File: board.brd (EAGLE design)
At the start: 52 x 53 mm, 14 parts, among them J1 5.5x2.1mm Barrel, T1 TIP122

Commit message: Updated with Gerber files
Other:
- board size 52 x 53 mm -> 52 x 51.7 mm
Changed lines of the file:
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@@
 <plain>
 <wire x1="0" y1="-12.7" x2="52.05" y2="-12.7" width="0" layer="20"/>
-<wire x1="52.05" y1="-12.7" x2="52.05" y2="40.31" width="0" layer="20"/>
-<wire x1="52.05" y1="40.31" x2="0" y2="40.31" width="0" layer="20"/>
-<wire x1="0" y1="40.31" x2="0" y2="-12.7" width="0" layer="20"/>
+<wire x1="52.05" y1="-12.7" x2="52.05" y2="39.04" width="0" layer="20"/>
+<wire x1="52.05" y1="39.04" x2="0" y2="39.04" width="0" layer="20"/>
+<wire x1="0" y1="39.04" x2="0" y2="-12.7" width="0" layer="20"/>
 </plain>
 <attributes>

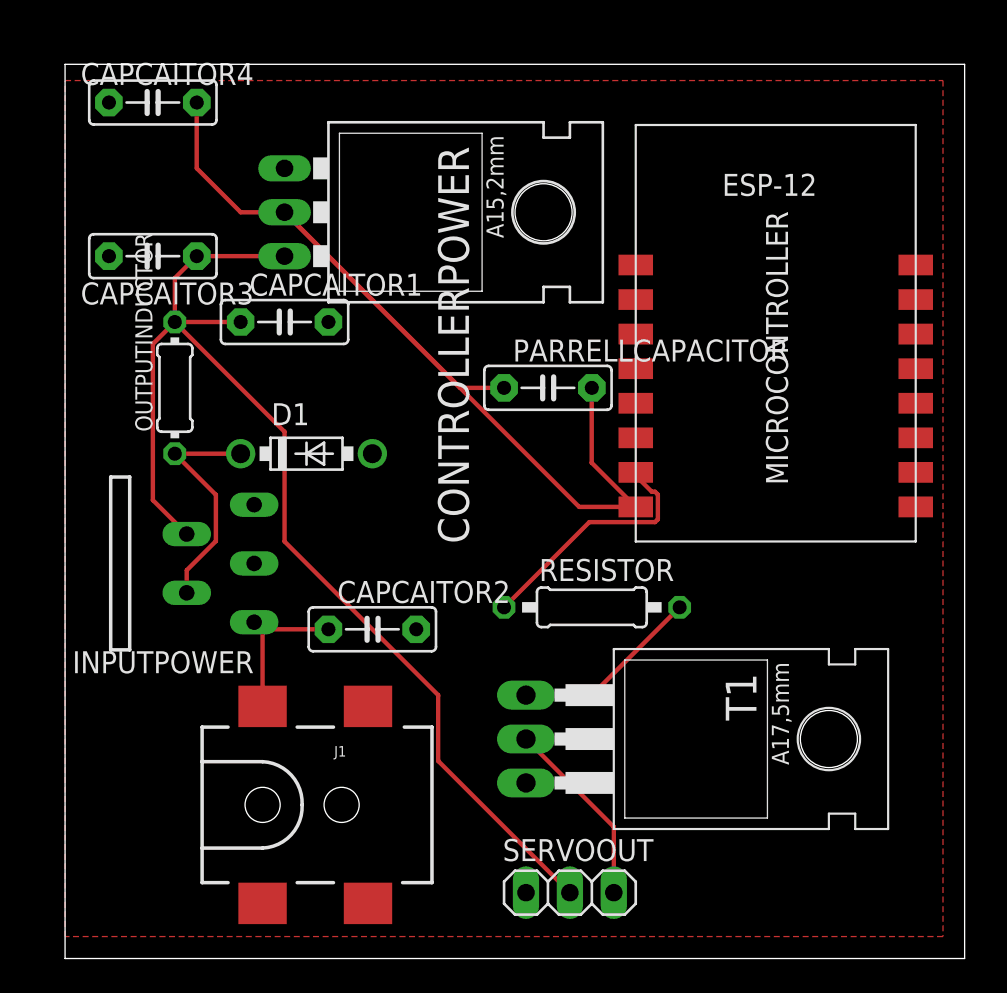
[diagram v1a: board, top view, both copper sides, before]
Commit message: Change base board to esp 01
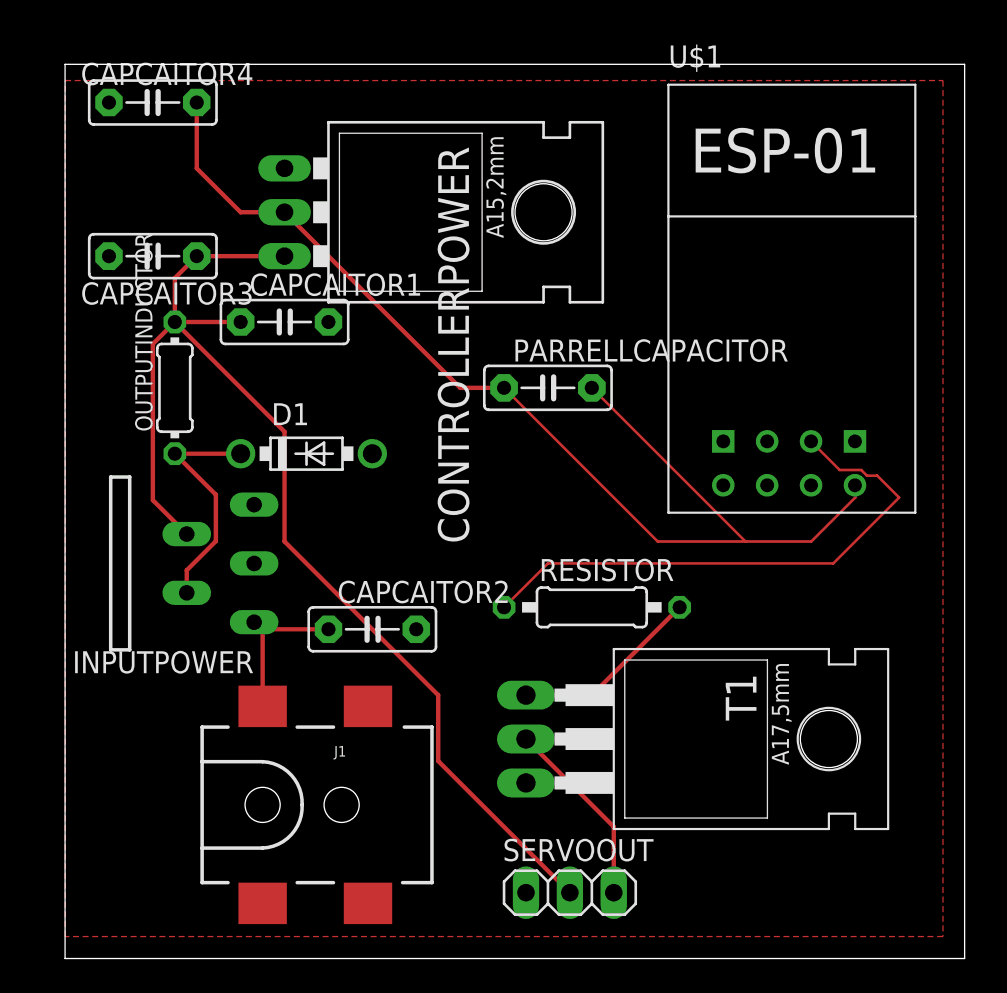
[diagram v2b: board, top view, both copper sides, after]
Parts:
- removed MICROCONTROLLER: ESP8266_ESP-12, ESP8266-ESP12:ESP8266-ESP12
- added U$1: ESP01, esp8266modules:ESP01
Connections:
- net GND: now also U$1.GND; no longer MICROCONTROLLER.1
- net N$7: now also U$1.VCC; no longer MICROCONTROLLER.16
- net N$9: now also U$1.GPIO0; no longer MICROCONTROLLER.15
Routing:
- net N$9: track 14.7 -> 31.9 mm
- net N$7: track 62.2 -> 65.2 mm
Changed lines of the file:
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@@
 <attribute name="VALUE" x="10.668" y="21.336" size="1.27" layer="27" ratio="10"/>
-</element>
-<element name="MICROCONTROLLER" library="ESP8266-ESP12" package="ESP8266-ESP12" value="ESP8266_ESP-12" x="33.02" y="11.43" smashed="yes">
-<attribute name="NAME" x="41.83" y="14.7" size="1.27" layer="21" rot="R90"/>
 </element>
 <element name="CONTROLLERPOWER" library="LD1117V33" package="LD1117V33" value="LD1117V33" x="21.59" y="30.48" smashed="yes" rot="R270">
@@
 <attribute name="VALUE" x="25.908" y="17.526" size="1.27" layer="27" ratio="10"/>
 </element>
+<element name="U$1" library="esp8266modules" package="ESP01" value="ESP01" x="41.91" y="22.86" smashed="yes">
+<attribute name="NAME" x="34.91" y="38.86" size="1.27" layer="25"/>
+<attribute name="VALUE" x="34.91" y="11.86" size="1.27" layer="27"/>
+</element>
 </elements>
 <signals>
@@
 <contactref element="CAPCAITOR3" pad="2"/>
 <contactref element="CAPCAITOR4" pad="2"/>
-<contactref element="MICROCONTROLLER" pad="1"/>
 <contactref element="SERVOOUT" pad="1"/>
 <contactref element="J1" pad="GND"/>
-<contactref element="T1" pad="3"/>
 <polygon width="0.254" layer="1">
 <vertex x="0" y="38.1"/>
@@
 </polygon>
 <contactref element="D1" pad="A"/>
+<contactref element="T1" pad="3"/>
+<contactref element="U$1" pad="GND"/>
 </signal>
 <signal name="N$3">
@@
 <contactref element="CONTROLLERPOWER" pad="OUT"/>
 <contactref element="CAPCAITOR4" pad="1"/>
-<contactref element="MICROCONTROLLER" pad="16"/>
 <wire x1="12.7" y1="30.48" x2="10.16" y2="30.48" width="0.254" layer="1"/>
 <wire x1="10.16" y1="30.48" x2="7.62" y2="33.02" width="0.254" layer="1"/>
 <wire x1="7.62" y1="33.02" x2="7.62" y2="36.83" width="0.254" layer="1"/>
 <contactref element="PARRELLCAPACITOR" pad="1"/>
-<contactref element="PARRELLCAPACITOR" pad="2"/>
-<wire x1="12.7" y1="30.48" x2="29.75" y2="13.43" width="0.254" layer="1"/>
-<wire x1="29.75" y1="13.43" x2="33.02" y2="13.43" width="0.254" layer="1"/>
 <wire x1="12.7" y1="30.48" x2="22.86" y2="20.32" width="0.254" layer="1"/>
 <wire x1="22.86" y1="20.32" x2="25.4" y2="20.32" width="0.254" layer="1"/>
-<wire x1="33.02" y1="13.43486875" x2="33.02" y2="13.43" width="0.254" layer="1"/>
-<wire x1="30.4706" y1="15.98426875" x2="33.02" y2="13.43486875" width="0.254" layer="1"/>
-<wire x1="30.48" y1="20.32" x2="30.4706" y2="20.3106" width="0.254" layer="1"/>
-<wire x1="30.4706" y1="20.3106" x2="30.4706" y2="15.98426875" width="0.254" layer="1"/>
+<contactref element="U$1" pad="VCC"/>
+<contactref element="PARRELLCAPACITOR" pad="2"/>
+<wire x1="30.48" y1="20.32" x2="39.37" y2="11.43" width="0.1524" layer="1"/>
+<wire x1="39.37" y1="11.43" x2="43.18" y2="11.43" width="0.1524" layer="1"/>
+<wire x1="43.18" y1="11.43" x2="45.72" y2="13.97" width="0.1524" layer="1"/>
+<wire x1="45.72" y1="13.97" x2="45.72" y2="14.6675" width="0.1524" layer="1"/>
+<wire x1="45.72" y1="14.6675" x2="45.705" y2="14.6825" width="0.1524" layer="1"/>
+<wire x1="25.4" y1="20.32" x2="34.29" y2="11.43" width="0.1524" layer="1"/>
+<wire x1="34.29" y1="11.43" x2="39.37" y2="11.43" width="0.1524" layer="1"/>
 </signal>
 <signal name="N$8">
@@
 <wire x1="26.67" y1="2.54" x2="30.48" y2="2.54" width="0.254" layer="1"/>
 </signal>
-<signal name="N$9">
-<contactref element="RESISTOR" pad="1"/>
-<contactref element="MICROCONTROLLER" pad="15"/>
-<wire x1="33.02" y1="15.43" x2="33.21" y2="15.43" width="0.254" layer="1"/>
-<wire x1="25.4" y1="7.81" x2="25.4" y2="7.62" width="0.254" layer="1"/>
-<wire x1="33.02" y1="15.43" x2="33.02" y2="15.24" width="0.254" layer="1"/>
-<wire x1="34.13573125" y1="14.3094" x2="34.2994" y2="14.14573125" width="0.254" layer="1"/>
-<wire x1="34.2994" y1="14.14573125" x2="34.2994" y2="12.71426875" width="0.254" layer="1"/>
-<wire x1="34.2994" y1="12.71426875" x2="34.13573125" y2="12.5506" width="0.254" layer="1"/>
-<wire x1="33.02" y1="15.24" x2="33.9506" y2="14.3094" width="0.254" layer="1"/>
-<wire x1="33.9506" y1="14.3094" x2="34.13573125" y2="14.3094" width="0.254" layer="1"/>
-<wire x1="30.3306" y1="12.5506" x2="25.4" y2="7.62" width="0.254" layer="1"/>
-<wire x1="34.13573125" y1="12.5506" x2="30.3306" y2="12.5506" width="0.254" layer="1"/>
-</signal>
 <signal name="N$10">
 <contactref element="T1" pad="2"/>
@@
 <wire x1="31.75" y1="-5.08" x2="31.75" y2="-8.89" width="0.254" layer="1"/>
 </signal>
+<signal name="N$9">
+<contactref element="RESISTOR" pad="1"/>
+<contactref element="U$1" pad="GPIO0"/>
+<wire x1="46.0705875" y1="15.5651" x2="46.3956875" y2="15.24" width="0.1524" layer="1"/>
+<wire x1="46.3956875" y1="15.24" x2="46.99" y2="15.24" width="0.1524" layer="1"/>
+<wire x1="43.165" y1="17.2225" x2="44.8224" y2="15.5651" width="0.1524" layer="1"/>
+<wire x1="44.8224" y1="15.5651" x2="46.0705875" y2="15.5651" width="0.1524" layer="1"/>
+<wire x1="46.99" y1="15.24" x2="48.26" y2="13.97" width="0.1524" layer="1"/>
+<wire x1="48.26" y1="13.97" x2="44.45" y2="10.16" width="0.1524" layer="1"/>
+<wire x1="44.45" y1="10.16" x2="27.94" y2="10.16" width="0.1524" layer="1"/>
+<wire x1="27.94" y1="10.16" x2="25.4" y2="7.62" width="0.1524" layer="1"/>
+</signal>
 </signals>

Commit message: Board update and autocad update to add nx files
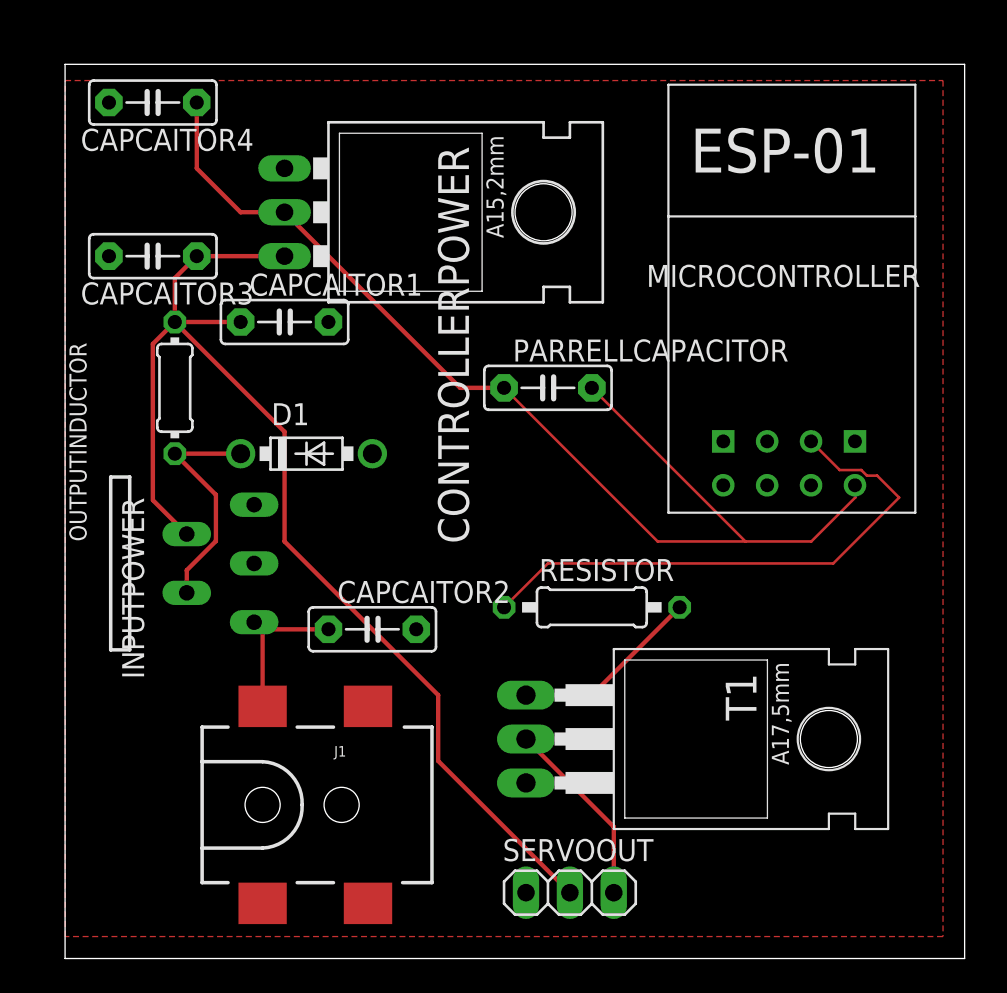
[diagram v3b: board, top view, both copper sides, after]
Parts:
- renumbered U$1 to MICROCONTROLLER
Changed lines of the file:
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@@
 <?xml version="1.0" encoding="utf-8"?>
 <!DOCTYPE eagle SYSTEM "eagle.dtd">
-<eagle version="9.2.2">
+<eagle version="9.2.0">
 <drawing>
 <settings>
@@
 </autorouter>
 <elements>
-<element name="INPUTPOWER" library="lm2575" package="TO220-5" value="LM2575-5.0T" x="2.54" y="10.16" smashed="yes" rot="R90">
-<attribute name="NAME" x="10.922" y="5.08" size="1.27" layer="25" rot="R180"/>
+<element name="INPUTPOWER" library="lm2575" package="TO220-5" value="LM2575-5.0T" x="2.54" y="10.16" rot="R90">
+<attribute name="NAME" x="3.302" y="13.97" size="1.27" layer="25" rot="R270"/>
 <attribute name="VALUE" x="12.192" y="16.51" size="1.27" layer="27" rot="R180"/>
 </element>
-<element name="CAPCAITOR2" library="capacitor-wima" library_urn="urn:adsk.eagle:library:116" package="C5B2.5" package3d_urn="urn:adsk.eagle:package:5426/1" value="100uf" x="17.78" y="6.35" smashed="yes">
+<element name="CAPCAITOR2" library="capacitor-wima" library_urn="urn:adsk.eagle:library:116" package="C5B2.5" package3d_urn="urn:adsk.eagle:package:5426/1" value="100uf" x="17.78" y="6.35">
 <attribute name="NAME" x="15.748" y="7.874" size="1.27" layer="25" ratio="10"/>
 <attribute name="VALUE" x="15.748" y="3.556" size="1.27" layer="27" ratio="10"/>
 </element>
-<element name="OUTPUTINDUCTOR" library="eagle-ltspice" library_urn="urn:adsk.eagle:library:217" package="0204/7" package3d_urn="urn:adsk.eagle:package:13274/1" value="330uH" x="6.35" y="20.32" smashed="yes" rot="R90">
-<attribute name="NAME" x="5.0546" y="17.78" size="0.9906" layer="25" ratio="10" rot="R90"/>
+<element name="OUTPUTINDUCTOR" library="eagle-ltspice" library_urn="urn:adsk.eagle:library:217" package="0204/7" package3d_urn="urn:adsk.eagle:package:13274/1" value="330uH" x="6.35" y="20.32" rot="R90">
+<attribute name="NAME" x="1.2446" y="11.43" size="0.9906" layer="25" ratio="10" rot="R90"/>
 <attribute name="SPICEMODEL" value="NONE" x="6.35" y="20.32" size="1.778" layer="27" rot="R90" display="off"/>
 <attribute name="SPICEPREFIX" value="L" x="6.35" y="20.32" size="1.778" layer="27" rot="R90" display="off"/>
 <attribute name="VALUE" x="6.8326" y="18.6944" size="0.9906" layer="27" ratio="10" rot="R90"/>
 </element>
-<element name="CAPCAITOR1" library="capacitor-wima" library_urn="urn:adsk.eagle:library:116" package="C5B2.5" package3d_urn="urn:adsk.eagle:package:5426/1" value="1000uf" x="12.7" y="24.13" smashed="yes">
+<element name="CAPCAITOR1" library="capacitor-wima" library_urn="urn:adsk.eagle:library:116" package="C5B2.5" package3d_urn="urn:adsk.eagle:package:5426/1" value="1000uf" x="12.7" y="24.13">
 <attribute name="NAME" x="10.668" y="25.654" size="1.27" layer="25" ratio="10"/>
 <attribute name="VALUE" x="10.668" y="21.336" size="1.27" layer="27" ratio="10"/>
 </element>
-<element name="CONTROLLERPOWER" library="LD1117V33" package="LD1117V33" value="LD1117V33" x="21.59" y="30.48" smashed="yes" rot="R270">
+<element name="CONTROLLERPOWER" library="LD1117V33" package="LD1117V33" value="LD1117V33" x="21.59" y="30.48" rot="R270">
 <attribute name="NAME" x="21.59" y="34.29" size="1.778" layer="25" ratio="10" rot="R270"/>
 <attribute name="VALUE" x="19.05" y="34.417" size="1.778" layer="27" ratio="10" rot="R270"/>
 </element>
-<element name="CAPCAITOR3" library="capacitor-wima" library_urn="urn:adsk.eagle:library:116" package="C5B2.5" package3d_urn="urn:adsk.eagle:package:5426/1" value="100nf" x="5.08" y="27.94" smashed="yes" rot="R180">
+<element name="CAPCAITOR3" library="capacitor-wima" library_urn="urn:adsk.eagle:library:116" package="C5B2.5" package3d_urn="urn:adsk.eagle:package:5426/1" value="100nf" x="5.08" y="27.94" rot="R180">
 <attribute name="NAME" x="10.922" y="26.416" size="1.27" layer="25" ratio="10" rot="R180"/>
 <attribute name="VALUE" x="7.112" y="30.734" size="1.27" layer="27" ratio="10" rot="R180"/>
 </element>
-<element name="CAPCAITOR4" library="capacitor-wima" library_urn="urn:adsk.eagle:library:116" package="C5B2.5" package3d_urn="urn:adsk.eagle:package:5426/1" value="10uf" x="5.08" y="36.83" smashed="yes" rot="R180">
-<attribute name="NAME" x="10.922" y="39.116" size="1.27" layer="25" ratio="10" rot="R180"/>
+<element name="CAPCAITOR4" library="capacitor-wima" library_urn="urn:adsk.eagle:library:116" package="C5B2.5" package3d_urn="urn:adsk.eagle:package:5426/1" value="10uf" x="5.08" y="36.83" rot="R180">
+<attribute name="NAME" x="10.922" y="35.306" size="1.27" layer="25" ratio="10" rot="R180"/>
 <attribute name="VALUE" x="7.112" y="37.084" size="1.27" layer="27" ratio="10" rot="R180"/>
 </element>
-<element name="SERVOOUT" library="pinhead" library_urn="urn:adsk.eagle:library:325" package="1X03" package3d_urn="urn:adsk.eagle:package:22458/2" value="" x="29.21" y="-8.89" smashed="yes">
+<element name="SERVOOUT" library="pinhead" library_urn="urn:adsk.eagle:library:325" package="1X03" package3d_urn="urn:adsk.eagle:package:22458/2" value="" x="29.21" y="-8.89">
 <attribute name="NAME" x="25.3238" y="-7.0612" size="1.27" layer="25" ratio="10"/>
 <attribute name="VALUE" x="25.4" y="-12.065" size="1.27" layer="27"/>
 </element>
-<element name="J1" library="SparkFun-Connectors" package="POWER_JACK_SMD" value="5.5x2.1mm Barrel" x="11.43" y="-3.81" smashed="yes">
+<element name="J1" library="SparkFun-Connectors" package="POWER_JACK_SMD" value="5.5x2.1mm Barrel" x="11.43" y="-3.81">
 <attribute name="NAME" x="15.5702" y="-1.016" size="0.6096" layer="25" font="vector" ratio="20"/>
 <attribute name="PROD_ID" value="CONN-08106" x="11.43" y="-3.81" size="1.778" layer="27" display="off"/>
@@
 <attribute name="VALUE" x="15.24" y="-7.112" size="0.6096" layer="27" font="vector" ratio="20"/>
 </element>
-<element name="T1" library="transistor" library_urn="urn:adsk.eagle:library:402" package="TO220" package3d_urn="urn:adsk.eagle:package:29897/1" value="TIP122" x="33.02" y="0" smashed="yes" rot="R270">
+<element name="T1" library="transistor" library_urn="urn:adsk.eagle:library:402" package="TO220" package3d_urn="urn:adsk.eagle:package:29897/1" value="TIP122" x="33.02" y="0" rot="R270">
 <attribute name="NAME" x="38.227" y="3.81" size="1.778" layer="25" ratio="10" rot="R270"/>
 <attribute name="VALUE" x="35.56" y="3.937" size="1.778" layer="27" ratio="10" rot="R270"/>
 </element>
-<element name="RESISTOR" library="eagle-ltspice" library_urn="urn:adsk.eagle:library:217" package="0207/10" package3d_urn="urn:adsk.eagle:package:13275/1" value="1000" x="30.48" y="7.62" smashed="yes">
+<element name="RESISTOR" library="eagle-ltspice" library_urn="urn:adsk.eagle:library:217" package="0207/10" package3d_urn="urn:adsk.eagle:package:13275/1" value="1000" x="30.48" y="7.62">
 <attribute name="NAME" x="27.432" y="9.144" size="1.27" layer="25" ratio="10"/>
 <attribute name="SPICEMODEL" value="NONE" x="30.48" y="7.62" size="1.778" layer="27" display="off"/>
@@
 <attribute name="VALUE" x="28.2194" y="6.985" size="1.27" layer="27" ratio="10"/>
 </element>
-<element name="D1" library="_mod_diode" package="DO41-7.6" value="1N5817-T" x="13.97" y="16.51" smashed="yes">
+<element name="D1" library="_mod_diode" package="DO41-7.6" value="1N5817-T" x="13.97" y="16.51">
 <attribute name="NAME" x="11.938" y="18.161" size="1.27" layer="25" ratio="10"/>
 <attribute name="VALUE" x="11.938" y="13.589" size="1.27" layer="27" ratio="10"/>
 </element>
-<element name="PARRELLCAPACITOR" library="capacitor-wima" library_urn="urn:adsk.eagle:library:116" package="C5B2.5" package3d_urn="urn:adsk.eagle:package:5426/1" value="01uf" x="27.94" y="20.32" smashed="yes">
+<element name="PARRELLCAPACITOR" library="capacitor-wima" library_urn="urn:adsk.eagle:library:116" package="C5B2.5" package3d_urn="urn:adsk.eagle:package:5426/1" value="01uf" x="27.94" y="20.32">
 <attribute name="NAME" x="25.908" y="21.844" size="1.27" layer="25" ratio="10"/>
 <attribute name="VALUE" x="25.908" y="17.526" size="1.27" layer="27" ratio="10"/>
 </element>
-<element name="U$1" library="esp8266modules" package="ESP01" value="ESP01" x="41.91" y="22.86" smashed="yes">
-<attribute name="NAME" x="34.91" y="38.86" size="1.27" layer="25"/>
+<element name="MICROCONTROLLER" library="esp8266modules" package="ESP01" value="ESP01" x="41.91" y="22.86">
+<attribute name="NAME" x="33.64" y="26.16" size="1.27" layer="25"/>
 <attribute name="VALUE" x="34.91" y="11.86" size="1.27" layer="27"/>
 </element>
@@
 <contactref element="D1" pad="A"/>
 <contactref element="T1" pad="3"/>
-<contactref element="U$1" pad="GND"/>
+<contactref element="MICROCONTROLLER" pad="GND"/>
 </signal>
 <signal name="N$3">
@@
 <wire x1="12.7" y1="30.48" x2="22.86" y2="20.32" width="0.254" layer="1"/>
 <wire x1="22.86" y1="20.32" x2="25.4" y2="20.32" width="0.254" layer="1"/>
-<contactref element="U$1" pad="VCC"/>
+<contactref element="MICROCONTROLLER" pad="VCC"/>
 <contactref element="PARRELLCAPACITOR" pad="2"/>
 <wire x1="30.48" y1="20.32" x2="39.37" y2="11.43" width="0.1524" layer="1"/>
@@
 <signal name="N$9">
 <contactref element="RESISTOR" pad="1"/>
-<contactref element="U$1" pad="GPIO0"/>
+<contactref element="MICROCONTROLLER" pad="GPIO0"/>
 <wire x1="46.0705875" y1="15.5651" x2="46.3956875" y2="15.24" width="0.1524" layer="1"/>
 <wire x1="46.3956875" y1="15.24" x2="46.99" y2="15.24" width="0.1524" layer="1"/>

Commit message: Updated PCB and Gerber Files
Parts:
- removed CAPCAITOR1: 1000uf, capacitor-wima:C5B2.5
- added 5REGCAP: 1000uf, capacitor-wima:C5B2.5
- renumbered CAPCAITOR2 to BATCAP, CAPCAITOR3 to 3REGCAP, CAPCAITOR4 to 3REGOUTCAP, CONTROLLERPOWER to 3VOLTREG, D1 to 5REGDIO, INPUTPOWER to 5VOLTREG, J1 to POWJACK, MICROCONTROLLER to MICROCONT, OUTPUTINDUCTOR to 5REGINDUC, PARRELLCAPACITOR to CONTCAP, RESISTOR to OUTREST, T1 to TRANOUT
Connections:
- net GND: now also 5REGCAP.2; no longer CAPCAITOR1.2
- net N$5: now also 5REGCAP.1; no longer CAPCAITOR1.1
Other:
- board size 52 x 51.7 mm -> 49.5 x 50.5 mm
